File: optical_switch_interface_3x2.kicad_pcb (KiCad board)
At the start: 2 copper layers, 69.8 x 40.6 mm, 1 part

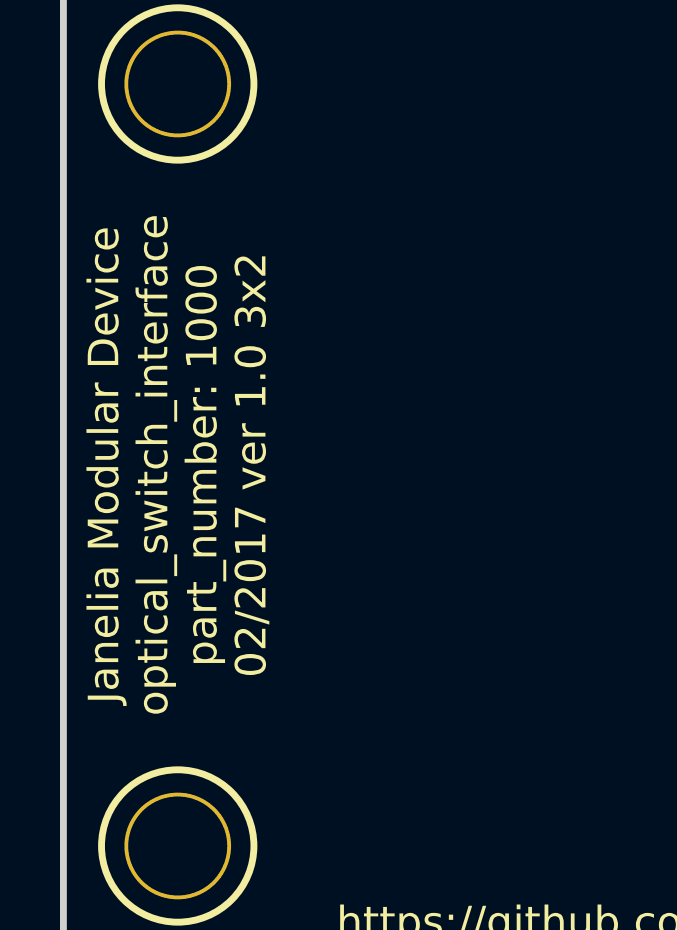
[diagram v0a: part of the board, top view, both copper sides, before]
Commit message: Added components and footprints.
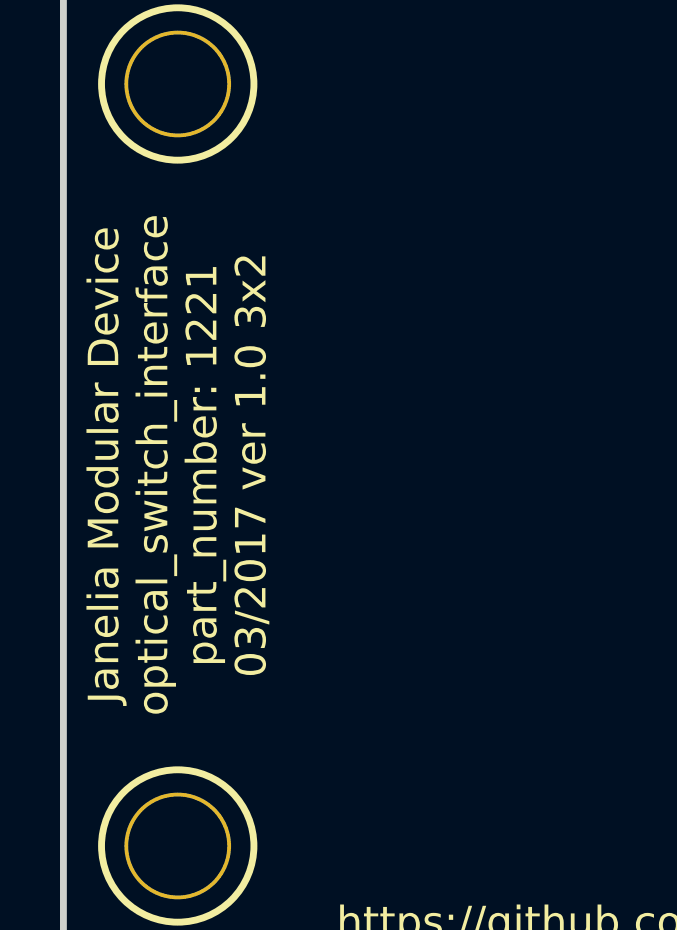
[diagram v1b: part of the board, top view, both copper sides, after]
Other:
- board text added: "Janelia Modular Device optical_switch_interface part_number: 1221 03/2017 ver 1.0 3x2"
- board text removed: "Janelia Modular Device optical_switch_interface part_number: 1000 02/2017 ver 1.0 3x2"
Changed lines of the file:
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@@
-(kicad_pcb (version 20170123) (host pcbnew no-vcs-found-7602~57~ubuntu16.04.1)
+(kicad_pcb (version 20170123) (host pcbnew no-vcs-found-6223534~58~ubuntu16.04.1)
   (general
     (links 0)
     (no_connects 0)
-    (area 0 0 0 0)
+    (area 85.356699 68.211699 155.943301 109.588301)
     (thickness 1.6)
     (drawings 6)
@@
     (effects (font (size 1.016 1.016) (thickness 0.1905)))
   )
-  (gr_text "Janelia Modular Device\noptical_switch_interface\npart_number: 1000\n02/2017 ver 1.0 3x2" (at 89.535 88.9 90) (layer F.SilkS)
+  (gr_text "Janelia Modular Device\noptical_switch_interface\npart_number: 1221\n03/2017 ver 1.0 3x2" (at 89.535 88.9 90) (layer F.SilkS)
     (effects (font (size 1.016 1.016) (thickness 0.254)))
   )

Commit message: Finished version 1.0.
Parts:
- added C1: 0.1uF, optical_switch_interface_3x2:SM1210, B.Cu at (130.8, 88.9)
- added P1: BNC_DOUBLE_RA, optical_switch_interface_3x2:BNC_DOUBLE, F.Cu at (149.9, 76.2)
- added P2: BNC_DOUBLE_RA, optical_switch_interface_3x2:BNC_DOUBLE, F.Cu at (149.9, 101.6)
- added P3: HEADER_01X05_SMD_SHR, optical_switch_interface_3x2:Header_Shrouded_5_Pin_SMD, F.Cu at (104.8, 81.9)
- added P4: HEADER_01X05_SMD_SHR, optical_switch_interface_3x2:Header_Shrouded_5_Pin_SMD, F.Cu at (125.1, 81.9)
- added P5: HEADER_01X05_SMD_SHR, optical_switch_interface_3x2:Header_Shrouded_5_Pin_SMD, F.Cu at (104.8, 95.9)
- added P6: HEADER_01X05_SMD_SHR, optical_switch_interface_3x2:Header_Shrouded_5_Pin_SMD, F.Cu at (125.1, 95.9)
- added R1: 180, optical_switch_interface_3x2:SM1210, B.Cu at (107.3, 81.9)
- added R2: 180, optical_switch_interface_3x2:SM1210, B.Cu at (127.6, 81.9)
- added R3: 180, optical_switch_interface_3x2:SM1210, B.Cu at (107.3, 95.9)
- added R4: 180, optical_switch_interface_3x2:SM1210, B.Cu at (127.6, 95.9)
- added U1: SN74ABT541BDWR, optical_switch_interface_3x2:SOIC_20, B.Cu at (141.0, 88.9)
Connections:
- MDB1 pad 2: (no net) -> /~ENABLE
- MDB1 pad 20: (no net) -> /OUT_0
- MDB1 pad 21: (no net) -> /OUT_1
- MDB1 pad 22: (no net) -> /OUT_2
- MDB1 pad 23: (no net) -> /OUT_3
- MDB1 pad 3: (no net) -> /IN_0
- MDB1 pad 4: (no net) -> /IN_1
- MDB1 pad 5: (no net) -> /IN_2
- MDB1 pad 6: (no net) -> /IN_3
- MDB1 pad GND: (no net) -> GND
- MDB1 pad VEE: (no net) -> VEE
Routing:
- net GND: track 0.00 -> 187.9 mm
- net /OUT_3: track 0.00 -> 112.1 mm
- net VEE: track 0.00 -> 102.2 mm, vias 0 -> 3
- net /OUT_2: track 0.00 -> 50.6 mm
- net /OUT_1: track 0.00 -> 46.0 mm
- net /~ENABLE: track 0.00 -> 43.6 mm, vias 0 -> 2
- net /IN_1: track 0.00 -> 41.5 mm
- net /OUT_0: track 0.00 -> 40.7 mm
- net /OUTPUT_1: track 0.00 -> 37.9 mm
- net /IN_3: track 0.00 -> 33.7 mm
- net /OUTPUT_0: track 0.00 -> 33.7 mm
- net /IN_2: track 0.00 -> 28.4 mm
- net /OUTPUT_3: track 0.00 -> 15.3 mm
- net /IN_0: track 0.00 -> 13.4 mm
- net /OUTPUT_2: track 0.00 -> 9.37 mm
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- added copper zone on B.Cu, net GND
- added copper zone on F.Cu, net GND
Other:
- net class GND: trace_width 0.4064 -> 0.8128
- net class SIGNAL: trace_width 0.4064 -> 0.8128
- board text added: "0"
- board text added: "1"
- board text added: "2"
- board text added: "3"
- board text added: "ANO"
- board text added: "BLK"
- board text added: "BLU"
- board text added: "CAT"
- board text added: "GND"
- board text added: "GRN"
- board text added: "OUT"
- board text added: "RED"
- board text added: "VEE"
- board text added: "WHT"
